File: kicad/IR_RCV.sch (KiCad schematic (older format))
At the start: 9 parts, among them J15 Host, J16 Slave, Q1 MTM231232LBF, Q2 DMN3065LW-7, Q3 SFH3015FA

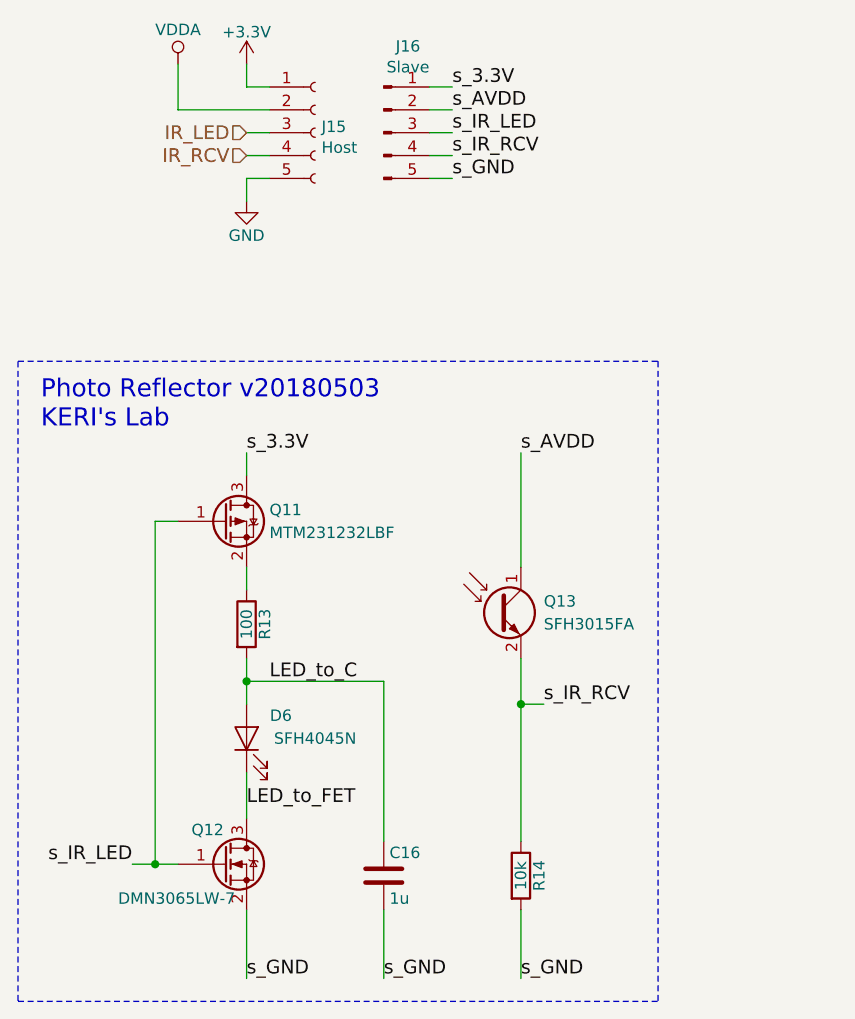
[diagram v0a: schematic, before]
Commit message: 部品を配置
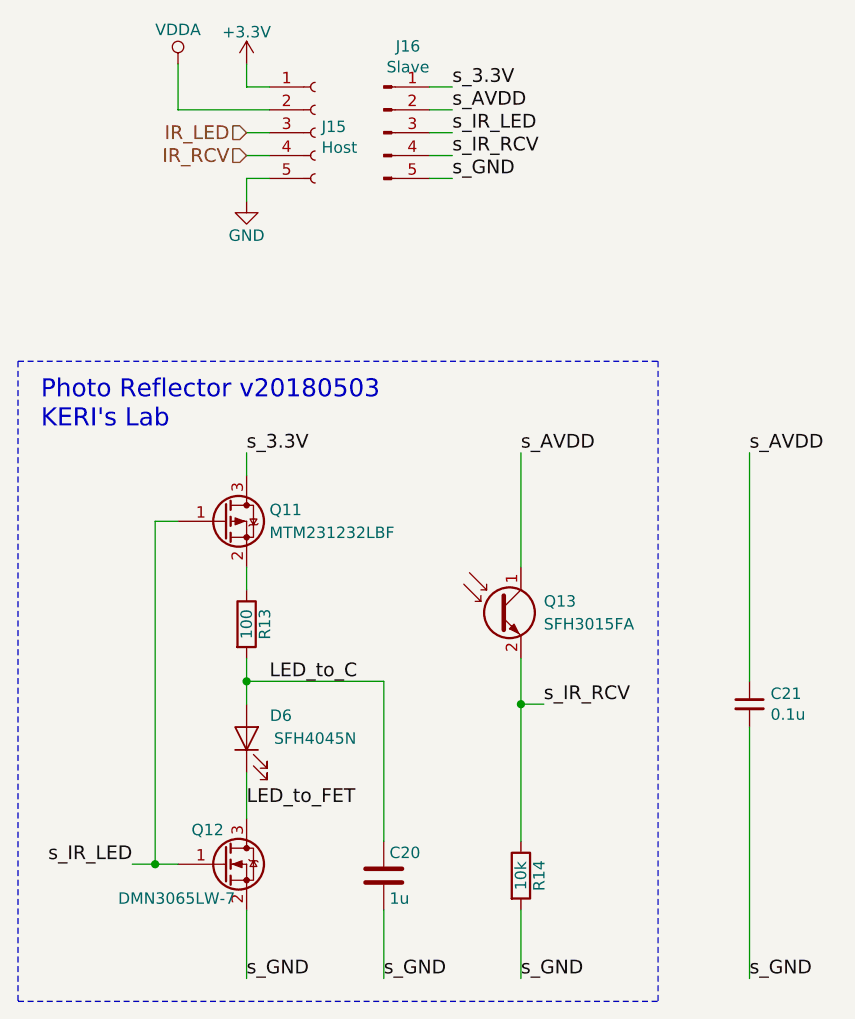
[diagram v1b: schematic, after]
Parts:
- added C12: 0.1u, Capacitor_SMD:C_0201_0603Metric, symbol Device:C_Small
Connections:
- net s_AVDD: now also C12.1
- net s_GND: now also C12.2
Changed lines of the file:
@@
 $Descr A4 11693 8268
 encoding utf-8
-Sheet 12 15
+Sheet 5 15
 Title ""
 Date ""
@@
 AR Path="/57CF0B09/589BF265" Ref="#PWR041"  Part="1"
 AR Path="/57CF2A30/589BF265" Ref="#PWR044"  Part="1"
-AR Path="/597E1B35/589BF265" Ref="#PWR060"  Part="1"
-AR Path="/597E1B39/589BF265" Ref="#PWR063"  Part="1"
-F 0 "#PWR063" H 4400 2350 50  0001 C CNN
+AR Path="/597E1B35/589BF265" Ref="#PWR062"  Part="1"
+AR Path="/597E1B39/589BF265" Ref="#PWR065"  Part="1"
+F 0 "#PWR065" H 4400 2350 50  0001 C CNN
 F 1 "GND" H 4400 2450 50  0000 C CNN
 F 2 "" H 4400 2600 50  0000 C CNN
@@
 AR Path="/57CF0B09/59C54857" Ref="#PWR039"  Part="1"
 AR Path="/57CF2A30/59C54857" Ref="#PWR042"  Part="1"
-AR Path="/597E1B35/59C54857" Ref="#PWR058"  Part="1"
-AR Path="/597E1B39/59C54857" Ref="#PWR061"  Part="1"
-F 0 "#PWR061" H 4100 1850 50  0001 C CNN
+AR Path="/597E1B35/59C54857" Ref="#PWR060"  Part="1"
+AR Path="/597E1B39/59C54857" Ref="#PWR063"  Part="1"
+F 0 "#PWR063" H 4100 1850 50  0001 C CNN
 F 1 "VDDA" H 4100 2150 50  0000 C CNN
 F 2 "" H 4100 2000 50  0001 C CNN
@@
 AR Path="/57CF0B09/5A172FEF" Ref="#PWR040"  Part="1"
 AR Path="/57CF2A30/5A172FEF" Ref="#PWR043"  Part="1"
-AR Path="/597E1B35/5A172FEF" Ref="#PWR059"  Part="1"
-AR Path="/597E1B39/5A172FEF" Ref="#PWR062"  Part="1"
-F 0 "#PWR062" H 4400 1850 50  0001 C CNN
+AR Path="/597E1B35/5A172FEF" Ref="#PWR061"  Part="1"
+AR Path="/597E1B39/5A172FEF" Ref="#PWR064"  Part="1"
+F 0 "#PWR064" H 4400 1850 50  0001 C CNN
 F 1 "+3.3V" H 4400 2140 50  0000 C CNN
 F 2 "" H 4400 2000 50  0001 C CNN
@@
 P 5000 5550
 AR Path="/57CF0B09/5A1B992B" Ref="C9"  Part="1"
-AR Path="/57CF2A30/5A1B992B" Ref="C10"  Part="1"
-AR Path="/597E1B35/5A1B992B" Ref="C15"  Part="1"
-AR Path="/597E1B39/5A1B992B" Ref="C16"  Part="1"
-F 0 "C16" H 5025 5650 50  0000 L CNN
+AR Path="/57CF2A30/5A1B992B" Ref="C11"  Part="1"
+AR Path="/597E1B35/5A1B992B" Ref="C18"  Part="1"
+AR Path="/597E1B39/5A1B992B" Ref="C20"  Part="1"
+F 0 "C20" H 5025 5650 50  0000 L CNN
 F 1 "1u" H 5025 5450 50  0000 L CNN
 F 2 "Capacitor_SMD:C_0402_1005Metric" H 5038 5400 50  0001 C CNN
@@
 	1    0    0    -1
 $EndComp
+$Comp
+L Device:C_Small C12
+U 1 1 5C29B79F
+P 6600 4800
+AR Path="/57CF2A30/5C29B79F" Ref="C12"  Part="1"
+AR Path="/57CF0B09/5C29B79F" Ref="C10"  Part="1"
+AR Path="/597E1B35/5C29B79F" Ref="C19"  Part="1"
+AR Path="/597E1B39/5C29B79F" Ref="C21"  Part="1"
+F 0 "C21" H 6692 4846 50  0000 L CNN
+F 1 "0.1u" H 6692 4755 50  0000 L CNN
+F 2 "Capacitor_SMD:C_0201_0603Metric" H 6600 4800 50  0001 C CNN
+F 3 "~" H 6600 4800 50  0001 C CNN
+	1    6600 4800
+	1    0    0    -1
+$EndComp
+Text Label 6600 6000 0    60   ~ 0
+s_GND
+Text Label 6600 3700 0    60   ~ 0
+s_AVDD
+Wire Wire Line
+	6600 3700 6600 4700
+Wire Wire Line
+	6600 4900 6600 6000
 $EndSCHEMATC

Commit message: リファレンスを除去
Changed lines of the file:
@@
 AR Path="/597E1B35/589BE75A" Ref="Q9"  Part="1"
 AR Path="/597E1B39/589BE75A" Ref="Q12"  Part="1"
-F 0 "Q12" H 4300 5650 50  0000 R CNN
+F 0 "Q2" H 4300 5650 50  0000 R CNN
 F 1 "DMN3065LW-7" H 4350 5350 50  0000 R CNN
 F 2 "TO_SOT_Packages_SMD:SOT-323_SC-70" H 4500 5600 50  0001 C CNN
@@
 AR Path="/597E1B35/589BE76D" Ref="R11"  Part="1"
 AR Path="/597E1B39/589BE76D" Ref="R13"  Part="1"
-F 0 "R13" V 4480 4450 50  0000 C CNN
+F 0 "R6" V 4480 4450 50  0000 C CNN
 F 1 "100" V 4400 4450 50  0000 C CNN
 F 2 "Resistor_SMD:R_0603_1608Metric" V 4330 4450 50  0001 C CNN
@@
 AR Path="/597E1B35/589BF265" Ref="#PWR062"  Part="1"
 AR Path="/597E1B39/589BF265" Ref="#PWR065"  Part="1"
-F 0 "#PWR065" H 4400 2350 50  0001 C CNN
+F 0 "#PWR041" H 4400 2350 50  0001 C CNN
 F 1 "GND" H 4400 2450 50  0000 C CNN
 F 2 "" H 4400 2600 50  0000 C CNN
@@
 AR Path="/597E1B35/594AC674" Ref="D5"  Part="1"
 AR Path="/597E1B39/594AC674" Ref="D6"  Part="1"
-F 0 "D6" V 4500 4800 50  0000 C CNN
+F 0 "D3" V 4500 4800 50  0000 C CNN
 F 1 "SFH4045N" V 4400 4650 50  0000 C CNN
 F 2 "mouse:SFH4045N" H 4400 4950 50  0001 C CNN
@@
 AR Path="/597E1B35/59C54857" Ref="#PWR060"  Part="1"
 AR Path="/597E1B39/59C54857" Ref="#PWR063"  Part="1"
-F 0 "#PWR063" H 4100 1850 50  0001 C CNN
+F 0 "#PWR039" H 4100 1850 50  0001 C CNN
 F 1 "VDDA" H 4100 2150 50  0000 C CNN
 F 2 "" H 4100 2000 50  0001 C CNN
@@
 AR Path="/597E1B35/5A172FEF" Ref="#PWR061"  Part="1"
 AR Path="/597E1B39/5A172FEF" Ref="#PWR064"  Part="1"
-F 0 "#PWR064" H 4400 1850 50  0001 C CNN
+F 0 "#PWR040" H 4400 1850 50  0001 C CNN
 F 1 "+3.3V" H 4400 2140 50  0000 C CNN
 F 2 "" H 4400 2000 50  0001 C CNN
@@
 AR Path="/597E1B35/5A1B992B" Ref="C18"  Part="1"
 AR Path="/597E1B39/5A1B992B" Ref="C20"  Part="1"
-F 0 "C20" H 5025 5650 50  0000 L CNN
+F 0 "C9" H 5025 5650 50  0000 L CNN
 F 1 "1u" H 5025 5450 50  0000 L CNN
 F 2 "Capacitor_SMD:C_0402_1005Metric" H 5038 5400 50  0001 C CNN
@@
 AR Path="/597E1B35/5A4ADF8B" Ref="Q10"  Part="1"
 AR Path="/597E1B39/5A4ADF8B" Ref="Q13"  Part="1"
-F 0 "Q13" H 5700 4450 50  0000 L CNN
+F 0 "Q3" H 5700 4450 50  0000 L CNN
 F 1 "SFH3015FA" H 5700 4350 50  0000 L CNN
 F 2 "mouse:SFH3015FA" H 5700 4500 50  0001 C CNN
@@
 AR Path="/597E1B35/589BEE3B" Ref="R12"  Part="1"
 AR Path="/597E1B39/589BEE3B" Ref="R14"  Part="1"
-F 0 "R14" V 5680 5550 50  0000 C CNN
+F 0 "R7" V 5680 5550 50  0000 C CNN
 F 1 "10k" V 5600 5550 50  0000 C CNN
 F 2 "Resistor_SMD:R_0201_0603Metric" V 5530 5550 50  0001 C CNN
@@
 AR Path="/597E1B35/5AB4DD07" Ref="Q8"  Part="1"
 AR Path="/597E1B39/5AB4DD07" Ref="Q11"  Part="1"
-F 0 "Q11" H 4500 4050 50  0000 L CNN
+F 0 "Q1" H 4500 4050 50  0000 L CNN
 F 1 "MTM231232LBF" H 4500 3950 50  0000 L CNN
 F 2 "TO_SOT_Packages_SMD:SOT-323_SC-70" H 4500 4100 50  0001 C CNN
@@
 AR Path="/57CF0B09/5B6F3B71" Ref="J3"  Part="1"
 AR Path="/57CF2A30/5B6F3B71" Ref="J5"  Part="1"
-F 0 "J15" H 4728 2326 50  0000 L CNN
+F 0 "J3" H 4728 2326 50  0000 L CNN
 F 1 "Host" H 4728 2235 50  0000 L CNN
 F 2 "mouse:STAND_HOST_05" H 4700 2300 50  0001 C CNN
@@
 AR Path="/57CF0B09/5B6F3C20" Ref="J4"  Part="1"
 AR Path="/57CF2A30/5B6F3C20" Ref="J6"  Part="1"
-F 0 "J16" H 5106 2678 50  0000 C CNN
+F 0 "J4" H 5106 2678 50  0000 C CNN
 F 1 "Slave" H 5106 2587 50  0000 C CNN
 F 2 "mouse:STAND_SLAVE_05" H 5000 2300 50  0001 C CNN
@@
 AR Path="/597E1B35/5C29B79F" Ref="C19"  Part="1"
 AR Path="/597E1B39/5C29B79F" Ref="C21"  Part="1"
-F 0 "C21" H 6692 4846 50  0000 L CNN
+F 0 "C10" H 6692 4846 50  0000 L CNN
 F 1 "0.1u" H 6692 4755 50  0000 L CNN
 F 2 "Capacitor_SMD:C_0201_0603Metric" H 6600 4800 50  0001 C CNN

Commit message: フットプリントを改良
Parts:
- Q1, Q2: footprint TO_SOT_Packages_SMD:SOT-323_SC-70 -> mouse:SOT-323_SC-70
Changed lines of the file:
@@
 AR Path="/597E1B35/589BE75A" Ref="Q9"  Part="1"
 AR Path="/597E1B39/589BE75A" Ref="Q12"  Part="1"
-F 0 "Q2" H 4300 5650 50  0000 R CNN
+F 0 "Q12" H 4300 5650 50  0000 R CNN
 F 1 "DMN3065LW-7" H 4350 5350 50  0000 R CNN
-F 2 "TO_SOT_Packages_SMD:SOT-323_SC-70" H 4500 5600 50  0001 C CNN
+F 2 "mouse:SOT-323_SC-70" H 4500 5600 50  0001 C CNN
 F 3 "" H 4300 5500 50  0000 C CNN
 	1    4300 5500
@@
 AR Path="/597E1B35/589BE76D" Ref="R11"  Part="1"
 AR Path="/597E1B39/589BE76D" Ref="R13"  Part="1"
-F 0 "R6" V 4480 4450 50  0000 C CNN
+F 0 "R13" V 4480 4450 50  0000 C CNN
 F 1 "100" V 4400 4450 50  0000 C CNN
 F 2 "Resistor_SMD:R_0603_1608Metric" V 4330 4450 50  0001 C CNN
@@
 AR Path="/597E1B35/589BF265" Ref="#PWR062"  Part="1"
 AR Path="/597E1B39/589BF265" Ref="#PWR065"  Part="1"
-F 0 "#PWR041" H 4400 2350 50  0001 C CNN
+F 0 "#PWR065" H 4400 2350 50  0001 C CNN
 F 1 "GND" H 4400 2450 50  0000 C CNN
 F 2 "" H 4400 2600 50  0000 C CNN
@@
 AR Path="/597E1B35/594AC674" Ref="D5"  Part="1"
 AR Path="/597E1B39/594AC674" Ref="D6"  Part="1"
-F 0 "D3" V 4500 4800 50  0000 C CNN
+F 0 "D6" V 4500 4800 50  0000 C CNN
 F 1 "SFH4045N" V 4400 4650 50  0000 C CNN
 F 2 "mouse:SFH4045N" H 4400 4950 50  0001 C CNN
@@
 AR Path="/597E1B35/59C54857" Ref="#PWR060"  Part="1"
 AR Path="/597E1B39/59C54857" Ref="#PWR063"  Part="1"
-F 0 "#PWR039" H 4100 1850 50  0001 C CNN
+F 0 "#PWR063" H 4100 1850 50  0001 C CNN
 F 1 "VDDA" H 4100 2150 50  0000 C CNN
 F 2 "" H 4100 2000 50  0001 C CNN
@@
 AR Path="/597E1B35/5A172FEF" Ref="#PWR061"  Part="1"
 AR Path="/597E1B39/5A172FEF" Ref="#PWR064"  Part="1"
-F 0 "#PWR040" H 4400 1850 50  0001 C CNN
+F 0 "#PWR064" H 4400 1850 50  0001 C CNN
 F 1 "+3.3V" H 4400 2140 50  0000 C CNN
 F 2 "" H 4400 2000 50  0001 C CNN
@@
 AR Path="/597E1B35/5A1B992B" Ref="C18"  Part="1"
 AR Path="/597E1B39/5A1B992B" Ref="C20"  Part="1"
-F 0 "C9" H 5025 5650 50  0000 L CNN
+F 0 "C20" H 5025 5650 50  0000 L CNN
 F 1 "1u" H 5025 5450 50  0000 L CNN
 F 2 "Capacitor_SMD:C_0402_1005Metric" H 5038 5400 50  0001 C CNN
@@
 AR Path="/597E1B35/5A4ADF8B" Ref="Q10"  Part="1"
 AR Path="/597E1B39/5A4ADF8B" Ref="Q13"  Part="1"
-F 0 "Q3" H 5700 4450 50  0000 L CNN
+F 0 "Q13" H 5700 4450 50  0000 L CNN
 F 1 "SFH3015FA" H 5700 4350 50  0000 L CNN
 F 2 "mouse:SFH3015FA" H 5700 4500 50  0001 C CNN
@@
 AR Path="/597E1B35/589BEE3B" Ref="R12"  Part="1"
 AR Path="/597E1B39/589BEE3B" Ref="R14"  Part="1"
-F 0 "R7" V 5680 5550 50  0000 C CNN
+F 0 "R14" V 5680 5550 50  0000 C CNN
 F 1 "10k" V 5600 5550 50  0000 C CNN
 F 2 "Resistor_SMD:R_0201_0603Metric" V 5530 5550 50  0001 C CNN
@@
 AR Path="/597E1B35/5AB4DD07" Ref="Q8"  Part="1"
 AR Path="/597E1B39/5AB4DD07" Ref="Q11"  Part="1"
-F 0 "Q1" H 4500 4050 50  0000 L CNN
+F 0 "Q11" H 4500 4050 50  0000 L CNN
 F 1 "MTM231232LBF" H 4500 3950 50  0000 L CNN
-F 2 "TO_SOT_Packages_SMD:SOT-323_SC-70" H 4500 4100 50  0001 C CNN
+F 2 "mouse:SOT-323_SC-70" H 4500 4100 50  0001 C CNN
 F 3 "" H 4300 4000 50  0001 C CNN
 	1    4300 4000
@@
 AR Path="/57CF0B09/5B6F3B71" Ref="J3"  Part="1"
 AR Path="/57CF2A30/5B6F3B71" Ref="J5"  Part="1"
-F 0 "J3" H 4728 2326 50  0000 L CNN
+F 0 "J15" H 4728 2326 50  0000 L CNN
 F 1 "Host" H 4728 2235 50  0000 L CNN
 F 2 "mouse:STAND_HOST_05" H 4700 2300 50  0001 C CNN
@@
 AR Path="/57CF0B09/5B6F3C20" Ref="J4"  Part="1"
 AR Path="/57CF2A30/5B6F3C20" Ref="J6"  Part="1"
-F 0 "J4" H 5106 2678 50  0000 C CNN
+F 0 "J16" H 5106 2678 50  0000 C CNN
 F 1 "Slave" H 5106 2587 50  0000 C CNN
 F 2 "mouse:STAND_SLAVE_05" H 5000 2300 50  0001 C CNN
@@
 AR Path="/597E1B35/5C29B79F" Ref="C19"  Part="1"
 AR Path="/597E1B39/5C29B79F" Ref="C21"  Part="1"
-F 0 "C10" H 6692 4846 50  0000 L CNN
+F 0 "C21" H 6692 4846 50  0000 L CNN
 F 1 "0.1u" H 6692 4755 50  0000 L CNN
 F 2 "Capacitor_SMD:C_0201_0603Metric" H 6600 4800 50  0001 C CNN
